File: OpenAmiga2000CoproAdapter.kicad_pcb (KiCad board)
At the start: 2 copper layers, 112 x 37.5 mm, 7 parts, among them CN1 A2000_COPRO_SLOT, P1 CONN_2, P2 CONN_2, P3 CONN_2, P4 CONN_2, P99 OSHW_LOGO, U1 68000D

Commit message: Add license info
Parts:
- moved P99 2.79 mm to (193.0, 120.8)
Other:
- board text added: "Licensed under CERN OHL v.1.2"
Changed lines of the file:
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@@
-(kicad_pcb (version 20171130) (host pcbnew 5.0.1)
+(kicad_pcb (version 20171130) (host pcbnew 5.0.2)
   (general
     (thickness 1.6)
-    (drawings 20)
+    (drawings 21)
     (tracks 339)
     (zones 0)
@@
   (title_block
     (title OpenAmiga2000CoproAdapter)
-    (date 2018-11-03)
-    (rev 1git)
+    (date 2019-02-11)
+    (rev 1)
     (company SukkoPera)
     (comment 1 "Based on work by Kipper2K")
+    (comment 2 "Licensed under CERN OHL v.1.2")
   )
   (layers
@@
   )
   (module Symbol:OSHW-Logo_7.5x8mm_Copper (layer B.Cu)
-    (at 193.04 123.571 180)
+    (at 193.04 120.777 180)
     (descr "Open Source Hardware Logo")
     (tags "Logo OSHW")
@@
       (xy 0.500964 3.601424)) (layer B.Cu) (width 0.01))
   )
+  (gr_text "Licensed under\nCERN OHL v.1.2" (at 193.04 128.778) (layer B.SilkS)
+    (effects (font (size 1 1) (thickness 0.15)) (justify mirror))
+  )
   (gr_text FC2/1/0 (at 141.478 116.332) (layer B.SilkS)

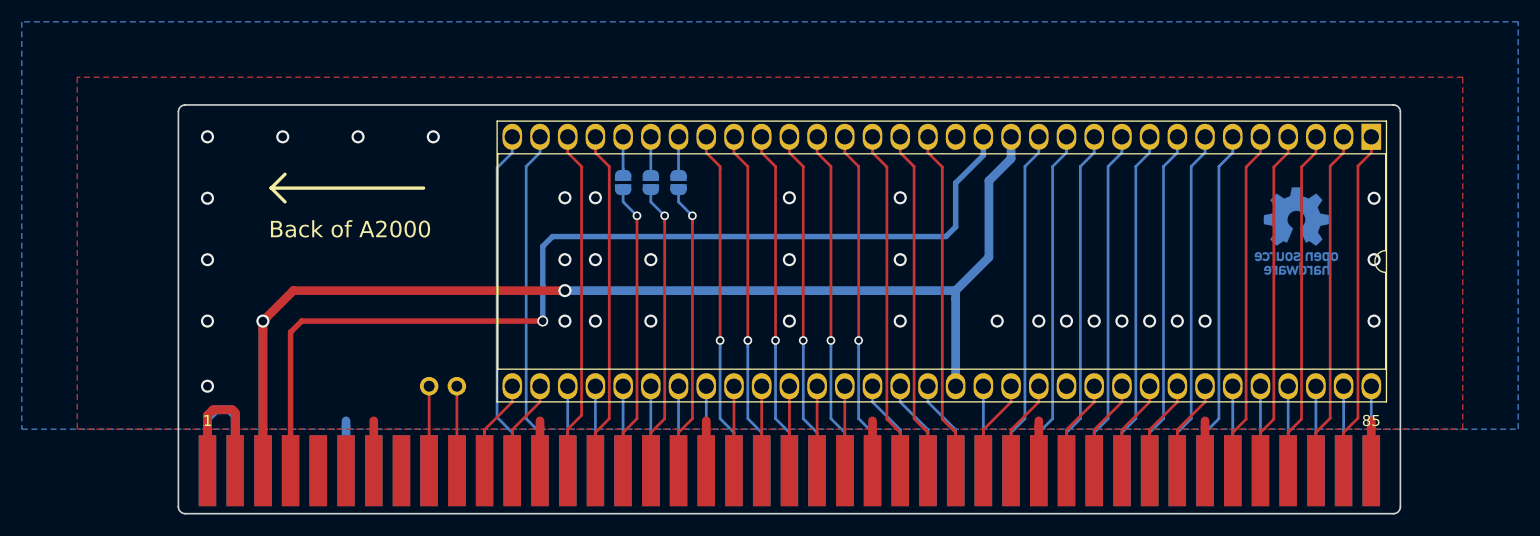
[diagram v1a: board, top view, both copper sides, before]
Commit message: Add pin names on silkscreen Yeah, I like this!
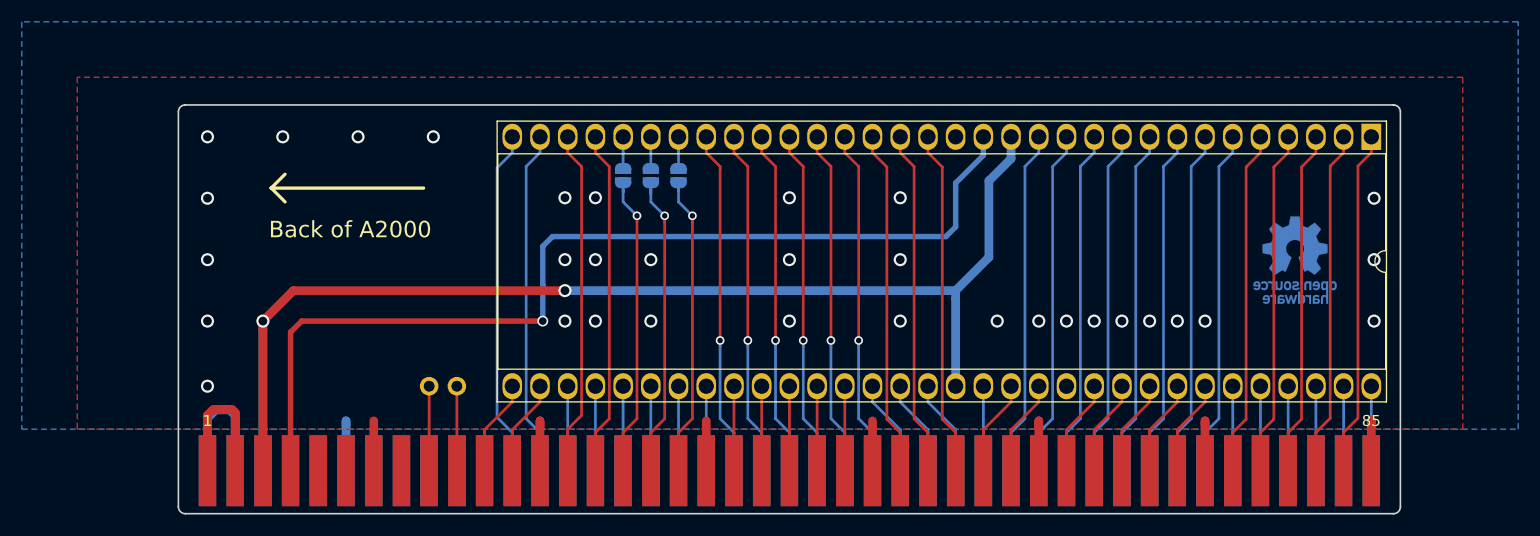
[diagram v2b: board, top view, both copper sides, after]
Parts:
- moved P99 2.67 mm to (192.9, 123.4)
- moved P2 0.63 mm to (136.4, 115.7)
- moved P3 0.63 mm to (133.9, 115.7)
- moved P4 0.63 mm to (131.3, 115.7)
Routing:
- net GND: track 62.8 -> 65.4 mm
- net /fc1: track 26.8 -> 27.8 mm
- net /fc0: track 26.8 -> 27.7 mm
- net /fc2: track 26.8 -> 27.6 mm
- net Net-(P4-Pad2): track 3.54 -> 2.91 mm
- net Net-(P3-Pad2): track 3.54 -> 2.91 mm
- net Net-(P2-Pad2): track 3.54 -> 2.91 mm
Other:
- board text added: "+5V"
- board text added: "A1"
- board text added: "A10"
- board text added: "A11"
- board text added: "A12"
- board text added: "A13"
- board text added: "A14"
- board text added: "A15"
- board text added: "A16"
- board text added: "A17"
- board text added: "A18"
- board text added: "A19"
- board text added: "A2"
- board text added: "A20"
- board text added: "A21"
- board text added: "A22"
- board text added: "A23"
- board text added: "A3"
- board text added: "A4"
- board text added: "A5"
- board text added: "A6"
- board text added: "A7"
- board text added: "A8"
- board text added: "A9"
- board text added: "CLK"
- board text added: "D0"
- board text added: "D1"
- board text added: "D10"
- board text added: "D11"
- board text added: "D12"
- board text added: "D13"
- board text added: "D14"
- board text added: "D15"
- board text added: "D2"
- board text added: "D3"
- board text added: "D4"
- board text added: "D5"
- board text added: "D6"
- board text added: "D7"
- board text added: "D8"
- board text added: "D9"
- board text added: "E"
- board text added: "FC0"
- board text added: "FC1"
- board text added: "FC2"
- board text added: "GND"
- board text added: "R/~W"
- board text added: "~AS"
- board text added: "~BERR"
- board text added: "~BG"
- board text added: "~BGACK"
- board text added: "~BR"
- board text added: "~DTACK"
- board text added: "~HALT"
- board text added: "~IPL0"
- board text added: "~IPL1"
- board text added: "~IPL2"
- board text added: "~LDS"
- board text added: "~RESET"
- board text added: "~UDS"
- board text added: "~VMA"
- board text added: "~VPA"
- board text removed: "FC2/1/0"

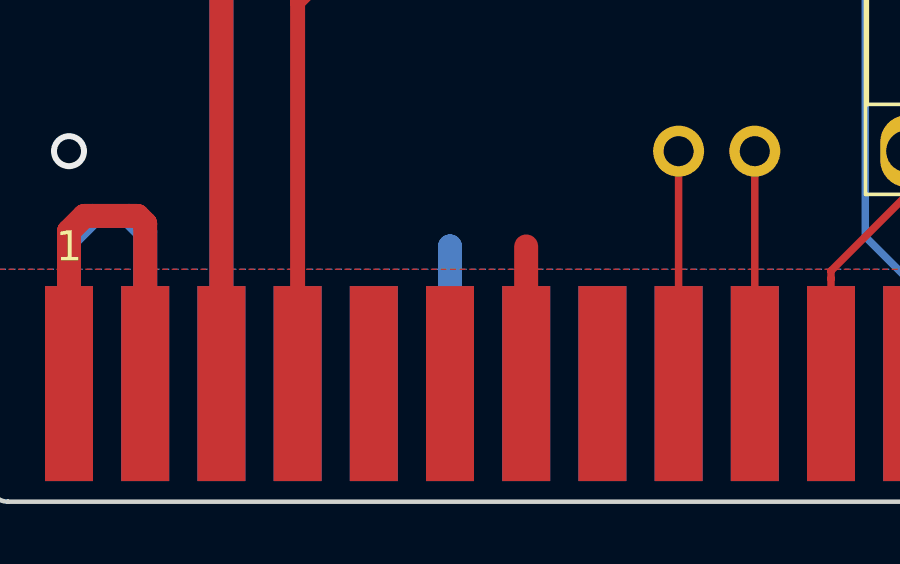
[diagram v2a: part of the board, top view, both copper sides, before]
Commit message: Treat CONFIG_IN pin properly
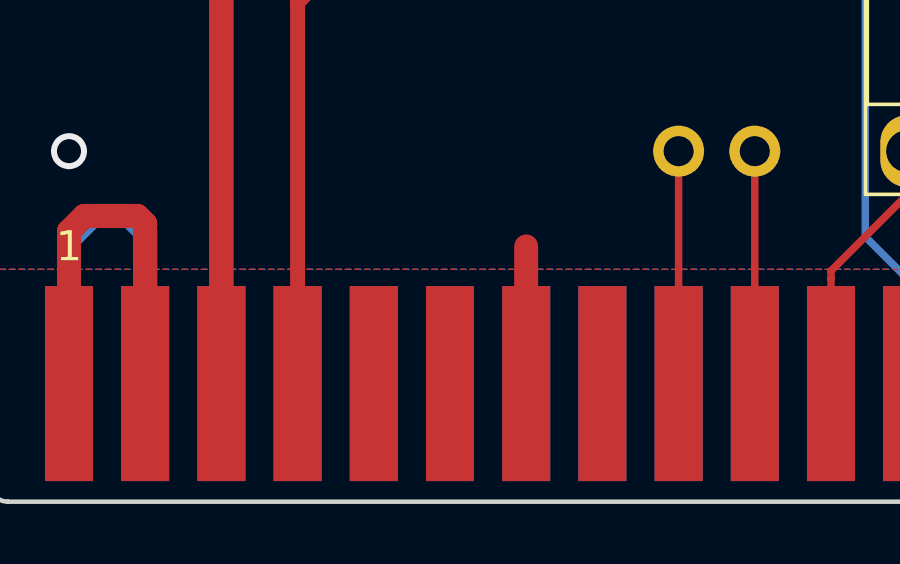
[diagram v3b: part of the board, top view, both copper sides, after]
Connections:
- CN1 pad 12: GND -> (no net)
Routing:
- net GND: track 65.4 -> 60.3 mm
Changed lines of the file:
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@@
     (thickness 1.6)
     (drawings 84)
-    (tracks 348)
+    (tracks 346)
     (zones 0)
     (modules 7)
@@
   (title_block
     (title OpenAmiga2000CoproAdapter)
-    (date 2019-02-13)
-    (rev 1)
+    (date 2019-02-14)
+    (rev 2git)
     (company SukkoPera)
     (comment 1 "Based on work by Kipper2K")
@@
     (pad 10 smd rect (at -10.16 -5.08) (size 1.6 6.5) (layers B.Cu B.Paste B.Mask))
     (pad 11 smd rect (at -7.62 -5.08) (size 1.6 6.5) (layers F.Cu F.Paste F.Mask))
-    (pad 12 smd rect (at -7.62 -5.08) (size 1.6 6.5) (layers B.Cu B.Paste B.Mask)
-      (net 1 GND))
+    (pad 12 smd rect (at -7.62 -5.08) (size 1.6 6.5) (layers B.Cu B.Paste B.Mask))
     (pad 13 smd rect (at -5.08 -5.08) (size 1.6 6.5) (layers F.Cu F.Paste F.Mask)
       (net 1 GND))
@@
   (via (at 93.218 117.771333) (size 1.2) (drill 0.8) (layers F.Cu B.Cu) (net 1))
   (segment (start 108.458 142.748) (end 108.458 138.176) (width 0.8) (layer F.Cu) (net 1) (status 10))
-  (segment (start 105.918 142.748) (end 105.918 138.176) (width 0.8) (layer B.Cu) (net 1) (status 10))
   (segment (start 199.898 142.748) (end 199.898 138.176) (width 0.8) (layer F.Cu) (net 1) (status 10))
   (segment (start 184.658 142.748) (end 184.658 138.176) (width 0.8) (layer F.Cu) (net 1) (status 10))
@@
   (via (at 200.152 123.401666) (size 1.2) (drill 0.8) (layers F.Cu B.Cu) (net 1))
   (via (at 184.658 129.032) (size 1.2) (drill 0.8) (layers F.Cu B.Cu) (net 1))
-  (segment (start 105.918 138.698) (end 105.918 138.176) (width 0.8) (layer B.Cu) (net 1))
   (segment (start 199.898 138.698) (end 199.898 138.176) (width 0.8) (layer F.Cu) (net 1))
   (segment (start 184.658 138.698) (end 184.658 138.176) (width 0.8) (layer F.Cu) (net 1))

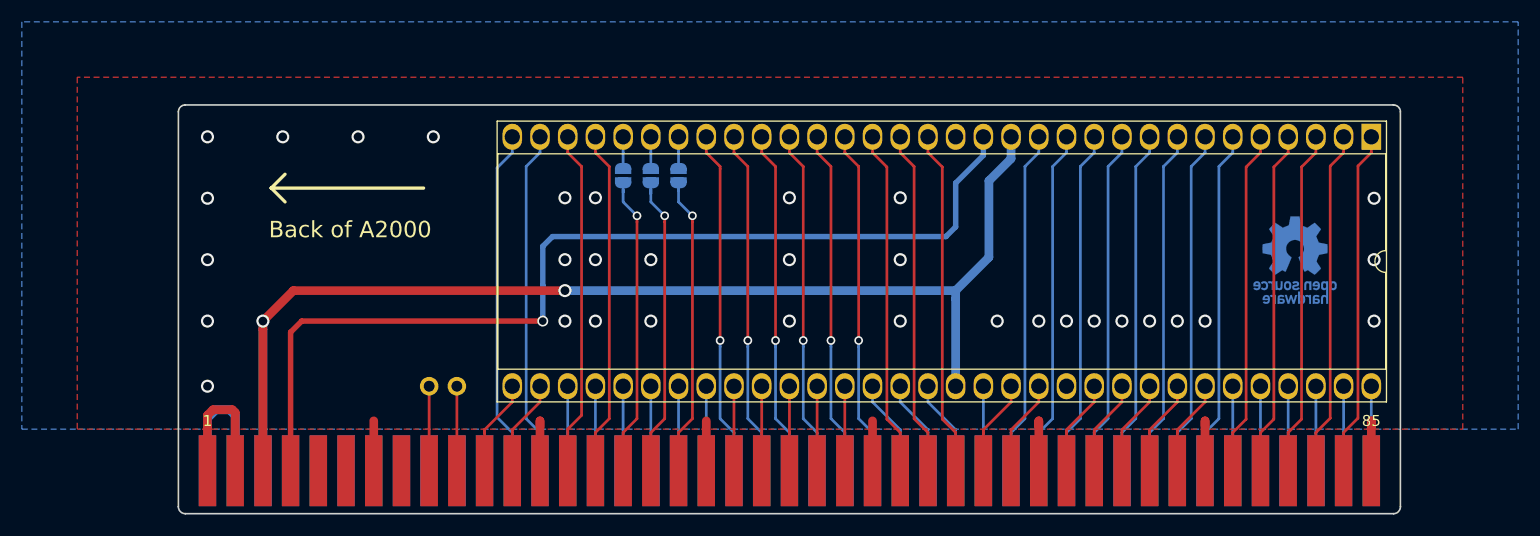
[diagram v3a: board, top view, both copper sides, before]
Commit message: Add test points for *all* the signals available on the connector
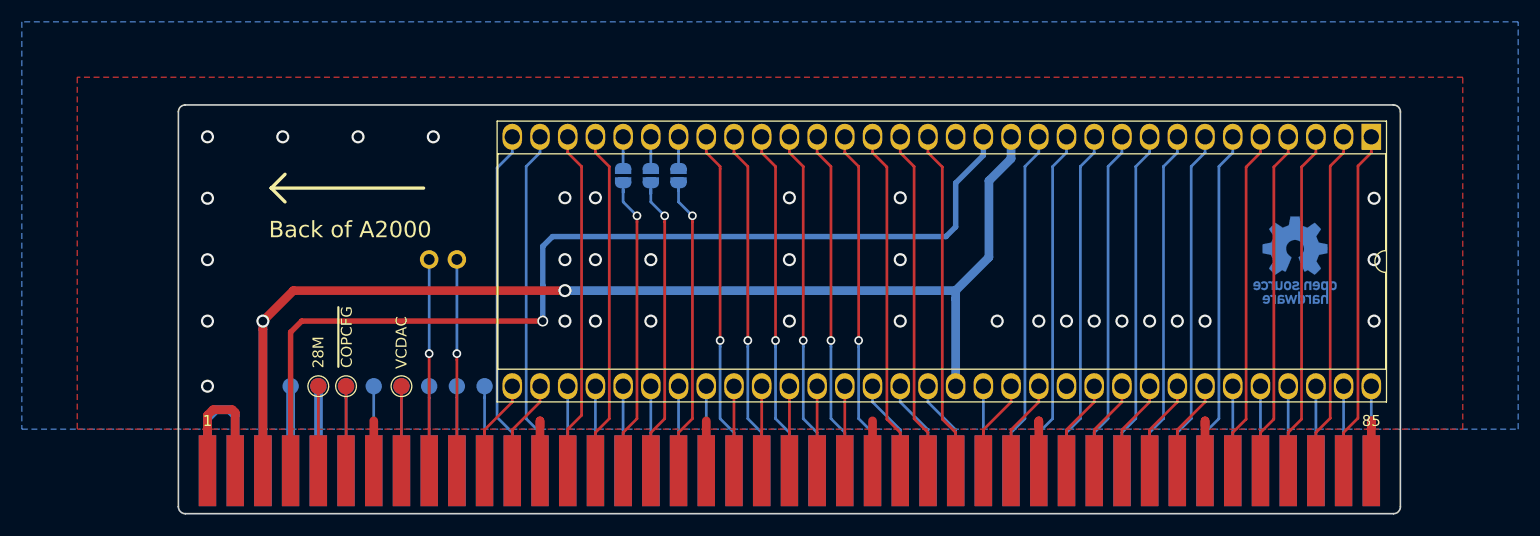
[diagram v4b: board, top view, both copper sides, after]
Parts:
- added P10: CONN_1, TestPoint:TestPoint_Pad_D1.5mm, B.Cu at (111.0, 135.0)
- added P11: CONN_1, TestPoint:TestPoint_Pad_D1.5mm, B.Cu at (113.5, 135.0)
- added P12: CONN_1, TestPoint:TestPoint_Pad_D1.5mm, B.Cu at (116.1, 135.0)
- added P13: CONN_1, TestPoint:TestPoint_Pad_D1.5mm, B.Cu at (118.6, 135.0)
- added P14: CONN_1, TestPoint:TestPoint_Pad_D1.5mm, B.Cu at (100.8, 135.0)
- added P15: CONN_1, TestPoint:TestPoint_Pad_D1.5mm, B.Cu at (103.4, 135.0)
- added P5: CONN_1, TestPoint:TestPoint_Pad_D1.5mm, F.Cu at (103.4, 135.0)
- added P6: CONN_1, TestPoint:TestPoint_Pad_D1.5mm, F.Cu at (105.9, 135.0)
- added P7: CONN_1, TestPoint:TestPoint_Pad_D1.5mm, F.Cu at (111.0, 135.0)
- added P8: CONN_1, TestPoint:TestPoint_Pad_D1.5mm, B.Cu at (105.9, 135.0)
- added P9: CONN_1, TestPoint:TestPoint_Pad_D1.5mm, B.Cu at (108.5, 135.0)
- moved P1 11.6 mm to (116.1, 123.4)
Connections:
- CN1 pad 10: (no net) -> +12V
- CN1 pad 11: (no net) -> Net-(CN1-Pad11)
- CN1 pad 12: (no net) -> Net-(CN1-Pad12)
- CN1 pad 14: (no net) -> Net-(CN1-Pad14)
- CN1 pad 15: (no net) -> Net-(CN1-Pad15)
- CN1 pad 16: (no net) -> Net-(CN1-Pad16)
- CN1 pad 18: (no net) -> Net-(CN1-Pad18)
- CN1 pad 20: (no net) -> Net-(CN1-Pad20)
- CN1 pad 22: (no net) -> Net-(CN1-Pad22)
- CN1 pad 8: (no net) -> -5V
- CN1 pad 9: (no net) -> Net-(CN1-Pad9)
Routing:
- net Net-(CN1-Pad19): track 7.75 -> 19.4 mm, vias 0 -> 1
- net Net-(CN1-Pad17): track 7.75 -> 19.4 mm, vias 0 -> 1
- net +12V: track 0.00 -> 7.76 mm
- net -5V: track 0.00 -> 7.75 mm
- net Net-(CN1-Pad9): track 0.00 -> 7.75 mm
- net Net-(CN1-Pad22): track 0.00 -> 7.75 mm
- net Net-(CN1-Pad20): track 0.00 -> 7.75 mm
- net Net-(CN1-Pad18): track 0.00 -> 7.75 mm
- net Net-(CN1-Pad16): track 0.00 -> 7.75 mm
- net Net-(CN1-Pad15): track 0.00 -> 7.75 mm
- net Net-(CN1-Pad14): track 0.00 -> 7.75 mm
- net Net-(CN1-Pad12): track 0.00 -> 7.75 mm
- net Net-(CN1-Pad11): track 0.00 -> 7.75 mm
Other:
- board text added: "+12V"
- board text added: "-5V"
- board text added: "28M"
- board text added: "V2"
- board text added: "VCDAC"
- board text added: "XRDY"
- board text added: "~BOSS"
- board text added: "~CFG_IN"
- board text added: "~COPCFG"
- board text added: "~INT6"
- board text added: "~VC1"
- board text added: "~VC3"
- board text removed: "V1"
